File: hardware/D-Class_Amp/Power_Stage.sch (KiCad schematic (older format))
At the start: 19 parts, among them Q301 PHP23NQ11T, Q302 PHP23NQ11T, Q303 PHP23NQ11T, Q304 PHP23NQ11T, U301 NCP1117-12_TO252, U302 IR21834, U303 IR21834

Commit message: updated SPWM model with new comparators, also added test points to schematic and fixed MOSFET footprints
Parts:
- Q301: footprint Package_TO_SOT_THT:TO-220-3_Vertical -> Package_TO_SOT_THT:TO-251-3-1EP_Horizontal_TabDown
- Q302, Q303, Q304: footprint Package_TO_SOT_THT:TO-220-3_Vertical -> Package_TO_SOT_THT:TO-251-3-1EP_Horizontal_TabD
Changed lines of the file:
@@
 $Descr A4 11693 8268
 encoding utf-8
-Sheet 3 5
+Sheet 5 5
 Title ""
 Date ""
@@
 F 0 "Q302" H 6038 1846 50  0000 L CNN
 F 1 "PHP23NQ11T" H 6038 1755 50  0000 L CNN
-F 2 "Package_TO_SOT_THT:TO-220-3_Vertical" H 5950 1900 50  0001 C CNN
+F 2 "Package_TO_SOT_THT:TO-251-3-1EP_Horizontal_TabD" H 5950 1900 50  0001 C CNN
 F 3 "https://assets.nexperia.com/documents/data-sheet/PHP23NQ11T.pdf" H 5750 1800 50  0001 C CNN
 	1    5750 1800
@@
 F 0 "Q301" H 6038 1346 50  0000 L CNN
 F 1 "PHP23NQ11T" H 6038 1255 50  0000 L CNN
-F 2 "Package_TO_SOT_THT:TO-220-3_Vertical" H 5950 1400 50  0001 C CNN
+F 2 "Package_TO_SOT_THT:TO-251-3-1EP_Horizontal_TabDown" H 5950 1400 50  0001 C CNN
 F 3 "https://assets.nexperia.com/documents/data-sheet/PHP23NQ11T.pdf" H 5750 1300 50  0001 C CNN
 	1    5750 1300
@@
 F 0 "Q303" H 8738 1346 50  0000 L CNN
 F 1 "PHP23NQ11T" H 8738 1255 50  0000 L CNN
-F 2 "Package_TO_SOT_THT:TO-220-3_Vertical" H 8650 1400 50  0001 C CNN
+F 2 "Package_TO_SOT_THT:TO-251-3-1EP_Horizontal_TabD" H 8650 1400 50  0001 C CNN
 F 3 "https://assets.nexperia.com/documents/data-sheet/PHP23NQ11T.pdf" H 8450 1300 50  0001 C CNN
 	1    8450 1300
@@
 F 0 "Q304" H 8738 1846 50  0000 L CNN
 F 1 "PHP23NQ11T" H 8738 1755 50  0000 L CNN
-F 2 "Package_TO_SOT_THT:TO-220-3_Vertical" H 8650 1900 50  0001 C CNN
+F 2 "Package_TO_SOT_THT:TO-251-3-1EP_Horizontal_TabD" H 8650 1900 50  0001 C CNN
 F 3 "https://assets.nexperia.com/documents/data-sheet/PHP23NQ11T.pdf" H 8450 1800 50  0001 C CNN
 	1    8450 1800

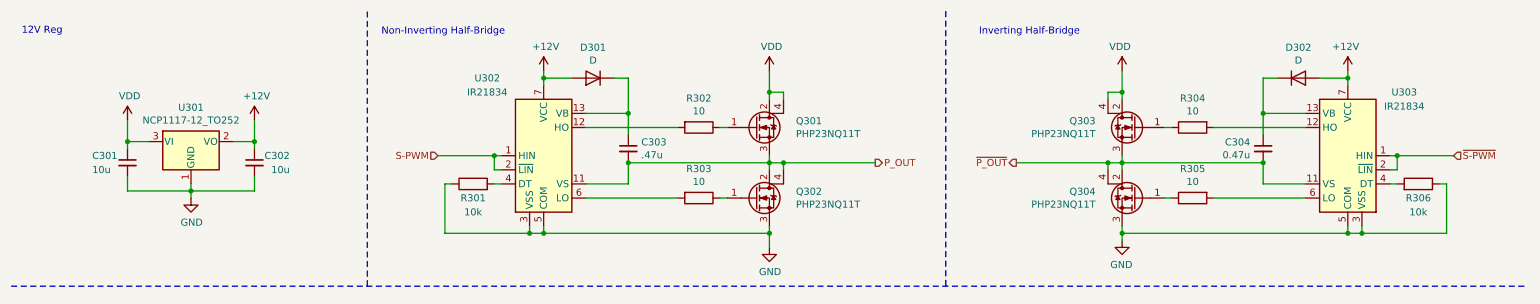
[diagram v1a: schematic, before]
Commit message: added the 5V regulator and updated footprints
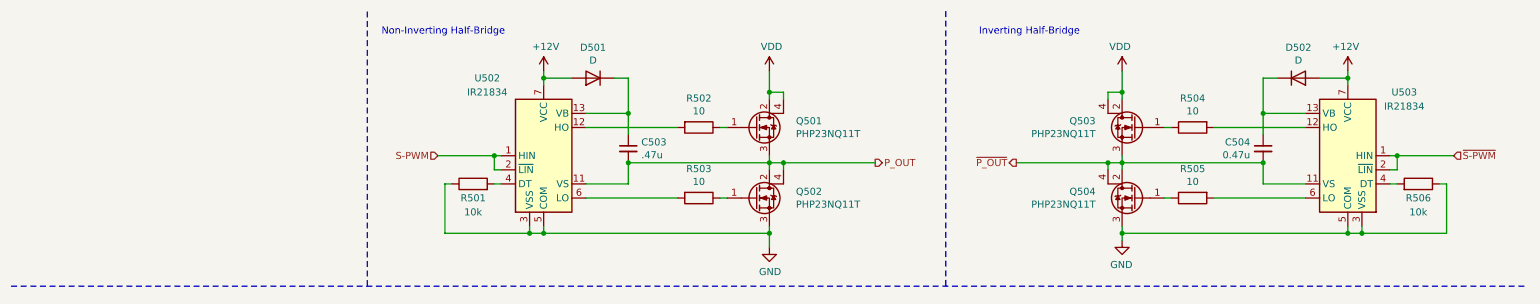
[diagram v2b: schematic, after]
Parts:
- removed C301, C302: 10u, Capacitor_SMD:C_0805_2012Metric_Pad1.18x1.45mm_HandSolder, symbol Device:C_Small
- removed U301: NCP1117-12_TO252, Package_TO_SOT_SMD:TO-252-2, symbol Regulator_Linear:NCP1117-12_TO252
- renumbered C303 to C503, C304 to C504, D301 to D501, D302 to D502, Q301 to Q501, Q302 to Q502, Q303 to Q503, Q304 to Q504, R301 to R501, R302 to R502, R303 to R503, R304 to R504, R305 to R505, R306 to R506, U302 to U502, U303 to U503
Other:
- note removed: "12V Reg\n\n"
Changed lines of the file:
@@
 $EndDescr
 $Comp
-L power:VDD #PWR0305
+L power:VDD #PWR0505
 U 1 1 6105D8A1
 P 5850 900
-F 0 "#PWR0305" H 5850 750 50  0001 C CNN
+F 0 "#PWR0505" H 5850 750 50  0001 C CNN
 F 1 "VDD" H 5865 1073 50  0000 C CNN
 F 2 "" H 5850 900 50  0001 C CNN
@@
 S-PWM
 $Comp
-L Device:C_Small C303
+L Device:C_Small C503
 U 1 1 610A4CCB
 P 4850 1450
-F 0 "C303" H 4942 1496 50  0000 L CNN
+F 0 "C503" H 4942 1496 50  0000 L CNN
 F 1 ".47u" H 4942 1405 50  0000 L CNN
 F 2 "Capacitor_SMD:C_0805_2012Metric_Pad1.18x1.45mm_HandSolder" H 4850 1450 50  0001 C CNN
@@
 $EndComp
 $Comp
-L power:+12V #PWR0304
+L power:+12V #PWR0504
 U 1 1 610ABD74
 P 4250 900
-F 0 "#PWR0304" H 4250 750 50  0001 C CNN
+F 0 "#PWR0504" H 4250 750 50  0001 C CNN
 F 1 "+12V" H 4265 1073 50  0000 C CNN
 F 2 "" H 4250 900 50  0001 C CNN
@@
 	3900 1500 3950 1500
 $Comp
-L Device:D D301
+L Device:D D501
 U 1 1 610CB2EC
 P 4600 950
-F 0 "D301" H 4600 733 50  0000 C CNN
+F 0 "D501" H 4600 733 50  0000 C CNN
 F 1 "D" H 4600 824 50  0000 C CNN
 F 2 "" H 4600 950 50  0001 C CNN
@@
 Non-Inverting Half-Bridge\n
 $Comp
-L Device:R R301
+L Device:R R501
 U 1 1 61055141
 P 3750 1700
-F 0 "R301" V 3650 1700 50  0000 C CNN
+F 0 "R501" V 3650 1700 50  0000 C CNN
 F 1 "10k" V 3550 1700 50  0000 C CNN
 F 2 "Resistor_SMD:R_0805_2012Metric_Pad1.20x1.40mm_HandSolder" V 3680 1700 50  0001 C CNN
@@
 $EndComp
 $Comp
-L Device:Q_NMOS_GDSD Q302
+L Device:Q_NMOS_GDSD Q502
 U 1 1 6104F394
 P 5750 1800
-F 0 "Q302" H 6038 1846 50  0000 L CNN
+F 0 "Q502" H 6038 1846 50  0000 L CNN
 F 1 "PHP23NQ11T" H 6038 1755 50  0000 L CNN
 F 2 "Package_TO_SOT_THT:TO-251-3-1EP_Horizontal_TabD" H 5950 1900 50  0001 C CNN
@@
 $EndComp
 $Comp
-L Device:Q_NMOS_GDSD Q301
+L Device:Q_NMOS_GDSD Q501
 U 1 1 6104F024
 P 5750 1300
-F 0 "Q301" H 6038 1346 50  0000 L CNN
+F 0 "Q501" H 6038 1346 50  0000 L CNN
 F 1 "PHP23NQ11T" H 6038 1255 50  0000 L CNN
 F 2 "Package_TO_SOT_THT:TO-251-3-1EP_Horizontal_TabDown" H 5950 1400 50  0001 C CNN
@@
 $EndComp
 $Comp
-L Driver_FET:IR21834 U302
+L Driver_FET:IR21834 U502
 U 1 1 6104C522
 P 4250 1500
-F 0 "U302" H 3850 2050 50  0000 C CNN
+F 0 "U502" H 3850 2050 50  0000 C CNN
 F 1 "IR21834" H 3850 1950 50  0000 C CNN
 F 2 "Package_SO:SOIC-14_3.9x8.7mm_P1.27mm" H 4250 1500 50  0001 C CIN
@@
 $EndComp
 $Comp
-L power:GND #PWR0306
+L power:GND #PWR0506
 U 1 1 6107E9DB
 P 5850 2150
-F 0 "#PWR0306" H 5850 1900 50  0001 C CNN
+F 0 "#PWR0506" H 5850 1900 50  0001 C CNN
 F 1 "GND" H 5855 1977 50  0000 C CNN
 F 2 "" H 5850 2150 50  0001 C CNN
@@
 	5850 2050 5850 2150
 $Comp
-L power:GND #PWR0308
+L power:GND #PWR0508
 U 1 1 610A1CEE
 P 8350 2100
-F 0 "#PWR0308" H 8350 1850 50  0001 C CNN
+F 0 "#PWR0508" H 8350 1850 50  0001 C CNN
 F 1 "GND" H 8355 1927 50  0000 C CNN
 F 2 "" H 8350 2100 50  0001 C CNN
@@
 $EndComp
 $Comp
-L Device:Q_NMOS_GDSD Q303
+L Device:Q_NMOS_GDSD Q503
 U 1 1 610F221C
 P 8450 1300
-F 0 "Q303" H 8738 1346 50  0000 L CNN
+F 0 "Q503" H 8738 1346 50  0000 L CNN
 F 1 "PHP23NQ11T" H 8738 1255 50  0000 L CNN
 F 2 "Package_TO_SOT_THT:TO-251-3-1EP_Horizontal_TabD" H 8650 1400 50  0001 C CNN
@@
 $EndComp
 $Comp
-L Device:Q_NMOS_GDSD Q304
+L Device:Q_NMOS_GDSD Q504
 U 1 1 610F2226
 P 8450 1800
-F 0 "Q304" H 8738 1846 50  0000 L CNN
+F 0 "Q504" H 8738 1846 50  0000 L CNN
 F 1 "PHP23NQ11T" H 8738 1755 50  0000 L CNN
 F 2 "Package_TO_SOT_THT:TO-251-3-1EP_Horizontal_TabD" H 8650 1900 50  0001 C CNN
@@
 $EndComp
 $Comp
-L Driver_FET:IR21834 U303
+L Driver_FET:IR21834 U503
 U 1 1 610F2212
 P 9950 1500
-F 0 "U303" H 9550 1950 50  0000 C CNN
+F 0 "U503" H 9550 1950 50  0000 C CNN
 F 1 "IR21834" H 9550 1850 50  0000 C CNN
 F 2 "Package_SO:SOIC-14_3.9x8.7mm_P1.27mm" H 9950 1500 50  0001 C CIN
@@
 $EndComp
 $Comp
-L Device:R R304
+L Device:R R504
 U 1 1 610F2230
 P 8850 1300
-F 0 "R304" V 8643 1300 50  0000 C CNN
+F 0 "R504" V 8643 1300 50  0000 C CNN
 F 1 "10" V 8734 1300 50  0000 C CNN
 F 2 "Resistor_SMD:R_0805_2012Metric_Pad1.20x1.40mm_HandSolder" V 8780 1300 50  0001 C CNN
@@
 	10250 1700 10300 1700
 $Comp
-L Device:D D302
+L Device:D D502
 U 1 1 610F2287
 P 9600 950
-F 0 "D302" H 9600 733 50  0000 C CNN
+F 0 "D502" H 9600 733 50  0000 C CNN
 F 1 "D" H 9600 824 50  0000 C CNN
 F 2 "" H 9600 950 50  0001 C CNN
@@
 	10700 1500 10300 1500
 $Comp
-L power:+12V #PWR0309
+L power:+12V #PWR0509
 U 1 1 610F2278
 P 9950 900
-F 0 "#PWR0309" H 9950 750 50  0001 C CNN
+F 0 "#PWR0509" H 9950 750 50  0001 C CNN
 F 1 "+12V" H 9965 1073 50  0000 C CNN
 F 2 "" H 9950 900 50  0001 C CNN
@@
 $EndComp
 $Comp
-L Device:C_Small C304
+L Device:C_Small C504
 U 1 1 610F226E
 P 9350 1450
-F 0 "C304" H 9442 1496 50  0000 L CNN
+F 0 "C504" H 9442 1496 50  0000 L CNN
 F 1 "0.47u" H 9442 1405 50  0000 L CNN
 F 2 "Capacitor_SMD:C_0805_2012Metric_Pad1.18x1.45mm_HandSolder" H 9350 1450 50  0001 C CNN
@@
 $EndComp
 $Comp
-L power:VDD #PWR0307
+L power:VDD #PWR0507
 U 1 1 610F224E
 P 8350 900
-F 0 "#PWR0307" H 8350 750 50  0001 C CNN
+F 0 "#PWR0507" H 8350 750 50  0001 C CNN
 F 1 "VDD" H 8365 1073 50  0000 C CNN
 F 2 "" H 8350 900 50  0001 C CNN
@@
 $EndComp
 $Comp
-L Device:R R306
+L Device:R R506
 U 1 1 610F2244
 P 10450 1700
-F 0 "R306" V 10350 1700 50  0000 C CNN
+F 0 "R506" V 10350 1700 50  0000 C CNN
 F 1 "10k" V 10250 1700 50  0000 C CNN
 F 2 "Resistor_SMD:R_0805_2012Metric_Pad1.20x1.40mm_HandSolder" V 10380 1700 50  0001 C CNN
@@
 $EndComp
 $Comp
-L Device:R R305
+L Device:R R505
 U 1 1 610F223A
 P 8850 1800
-F 0 "R305" V 8643 1800 50  0000 C CNN
+F 0 "R505" V 8643 1800 50  0000 C CNN
 F 1 "10" V 8734 1800 50  0000 C CNN
 F 2 "Resistor_SMD:R_0805_2012Metric_Pad1.20x1.40mm_HandSolder" V 8780 1800 50  0001 C CNN
@@
 Wire Wire Line
 	3550 2050 4150 2050
-$Comp
-L Regulator_Linear:NCP1117-12_TO252 U301
-U 1 1 61102BEC
-P 1750 1400
-F 0 "U301" H 1750 1642 50  0000 C CNN
-F 1 "NCP1117-12_TO252" H 1750 1551 50  0000 C CNN
-F 2 "Package_TO_SOT_SMD:TO-252-2" H 1750 1625 50  0001 C CNN
-F 3 "http://www.onsemi.com/pub_link/Collateral/NCP1117-D.PDF" H 1750 1400 50  0001 C CNN
-	1    1750 1400
-	1    0    0    -1
-$EndComp
-$Comp
-L power:+12V #PWR0303
-U 1 1 61106009
-P 2200 1250
-F 0 "#PWR0303" H 2200 1100 50  0001 C CNN
-F 1 "+12V" H 2215 1423 50  0000 C CNN
-F 2 "" H 2200 1250 50  0001 C CNN
-F 3 "" H 2200 1250 50  0001 C CNN
-	1    2200 1250
-	1    0    0    -1
-$EndComp
-$Comp
-L power:VDD #PWR0301
-U 1 1 61109C5A
-P 1300 1250
-F 0 "#PWR0301" H 1300 1100 50  0001 C CNN
-F 1 "VDD" H 1315 1423 50  0000 C CNN
-F 2 "" H 1300 1250 50  0001 C CNN
-F 3 "" H 1300 1250 50  0001 C CNN
-	1    1300 1250
-	1    0    0    -1
-$EndComp
-$Comp
-L power:GND #PWR0302
-U 1 1 6110DE87
-P 1750 1800
-F 0 "#PWR0302" H 1750 1550 50  0001 C CNN
-F 1 "GND" H 1755 1627 50  0000 C CNN
-F 2 "" H 1750 1800 50  0001 C CNN
-F 3 "" H 1750 1800 50  0001 C CNN
-	1    1750 1800
-	1    0    0    -1
-$EndComp
-Wire Wire Line
-	1750 1700 1750 1750
-Connection ~ 1750 1750
-Wire Wire Line
-	1750 1750 1750 1800
-Wire Wire Line
-	2200 1400 2200 1250
-Connection ~ 2200 1400
-Wire Wire Line
-	2200 1750 1750 1750
-Wire Wire Line
-	2050 1400 2200 1400
-Wire Wire Line
-	2200 1650 2200 1750
-Wire Wire Line
-	2200 1400 2200 1450
-Wire Wire Line
-	1300 1400 1450 1400
-Wire Wire Line
-	1300 1400 1300 1250
-Wire Wire Line
-	1300 1400 1300 1450
-Connection ~ 1300 1400
-Wire Wire Line
-	1300 1650 1300 1750
-$Comp
-L Device:C_Small C301
-U 1 1 6116A646
-P 1300 1550
-F 0 "C301" H 1050 1600 50  0000 L CNN
-F 1 "10u" H 1050 1500 50  0000 L CNN
-F 2 "Capacitor_SMD:C_0805_2012Metric_Pad1.18x1.45mm_HandSolder" H 1300 1550 50  0001 C CNN
-F 3 "~" H 1300 1550 50  0001 C CNN
-	1    1300 1550
-	1    0    0    -1
-$EndComp
-$Comp
-L Device:C_Small C302
-U 1 1 6116D137
-P 2200 1550
-F 0 "C302" H 1950 1600 50  0000 L CNN
-F 1 "10u" H 1950 1500 50  0000 L CNN
-F 2 "Capacitor_SMD:C_0805_2012Metric_Pad1.18x1.45mm_HandSolder" H 2200 1550 50  0001 C CNN
-F 3 "~" H 2200 1550 50  0001 C CNN
-	1    2200 1550
-	-1   0    0    -1
-$EndComp
 Text HLabel 6600 1550 2    50   Output ~ 0
 P_OUT
@@
 Wire Notes Line
 	475  2425 11225 2425
-Text Notes 550  725  0    50   ~ 0
-12V Reg\n\n
-Wire Wire Line
-	1300 1750 1750 1750
-$Comp
-L Device:R R303
+$Comp
+L Device:R R503
 U 1 1 610540BF
 P 5350 1800
-F 0 "R303" V 5143 1800 50  0000 C CNN
+F 0 "R503" V 5143 1800 50  0000 C CNN
 F 1 "10" V 5234 1800 50  0000 C CNN
 F 2 "Resistor_SMD:R_0805_2012Metric_Pad1.20x1.40mm_HandSolder" V 5280 1800 50  0001 C CNN
@@
 $EndComp
 $Comp
-L Device:R R302
+L Device:R R502
 U 1 1 61051377
 P 5350 1300
-F 0 "R302" V 5143 1300 50  0000 C CNN
+F 0 "R502" V 5143 1300 50  0000 C CNN
 F 1 "10" V 5234 1300 50  0000 C CNN
 F 2 "Resistor_SMD:R_0805_2012Metric_Pad1.20x1.40mm_HandSolder" V 5280 1300 50  0001 C CNN

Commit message: supply cap and design notes
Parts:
- added C501, C502: 10u, Capacitor_SMD:C_0805_2012Metric_Pad1.18x1.45mm_HandSolder, symbol Device:C_Small
- U502, U503: Digikey (none) -> IR21834SPBFDKR-ND
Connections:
- net +12V: now also C501.1, C502.1
- net GND: now also C501.2, C502.2
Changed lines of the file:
@@
 U 1 1 6104C522
 P 4250 1500
-F 0 "U502" H 3850 2050 50  0000 C CNN
-F 1 "IR21834" H 3850 1950 50  0000 C CNN
+F 0 "U502" H 3850 1950 50  0000 C CNN
+F 1 "IR21834" H 3850 1875 50  0000 C CNN
 F 2 "Package_SO:SOIC-14_3.9x8.7mm_P1.27mm" H 4250 1500 50  0001 C CIN
 F 3 "https://www.infineon.com/dgdl/ir2183.pdf?fileId=5546d462533600a4015355c9490e16d1" H 4250 1500 50  0001 C CNN
+F 4 "IR21834SPBFDKR-ND" H 4250 1500 50  0001 C CNN "Digikey"
 	1    4250 1500
 	1    0    0    -1
@@
 F 2 "Package_SO:SOIC-14_3.9x8.7mm_P1.27mm" H 9950 1500 50  0001 C CIN
 F 3 "https://www.infineon.com/dgdl/ir2183.pdf?fileId=5546d462533600a4015355c9490e16d1" H 9950 1500 50  0001 C CNN
+F 4 "IR21834SPBFDKR-ND" H 9950 1500 50  0001 C CNN "Digikey"
 	1    9950 1500
 	-1   0    0    -1
@@
 Wire Notes Line
 	7100 475  7100 2425
-Wire Notes Line
-	475  2425 11225 2425
 $Comp
 L Device:R R503
@@
 	0    1    1    0
 $EndComp
+$Comp
+L Device:C_Small C501
+U 1 1 61139FFD
+P 3550 1300
+F 0 "C501" H 3642 1346 50  0000 L CNN
+F 1 "10u" H 3642 1255 50  0000 L CNN
+F 2 "Capacitor_SMD:C_0805_2012Metric_Pad1.18x1.45mm_HandSolder" H 3550 1300 50  0001 C CNN
+F 3 "~" H 3550 1300 50  0001 C CNN
+	1    3550 1300
+	-1   0    0    -1
+$EndComp
+$Comp
+L Device:C_Small C502
+U 1 1 6113D2CB
+P 10650 1300
+F 0 "C502" H 10742 1346 50  0000 L CNN
+F 1 "10u" H 10742 1255 50  0000 L CNN
+F 2 "Capacitor_SMD:C_0805_2012Metric_Pad1.18x1.45mm_HandSolder" H 10650 1300 50  0001 C CNN
+F 3 "~" H 10650 1300 50  0001 C CNN
+	1    10650 1300
+	1    0    0    -1
+$EndComp
+Wire Wire Line
+	10650 1700 10650 1400
+Connection ~ 10650 1700
+Wire Wire Line
+	10650 1225 10650 1200
+Connection ~ 10650 1200
+Wire Wire Line
+	10650 1200 10650 950
+Wire Wire Line
+	9950 950  10650 950
+Wire Wire Line
+	3550 1700 3550 1400
+Connection ~ 3550 1700
+Wire Wire Line
+	3550 1200 3550 950
+Wire Wire Line
+	3550 950  4250 950
+Wire Notes Line
+	3000 2450 11225 2450
+Wire Notes Line
+	11225 2450 11225 2475
 $EndSCHEMATC
